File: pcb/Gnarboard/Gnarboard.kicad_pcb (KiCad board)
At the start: 2 copper layers, 184 x 136 mm, 134 parts, among them J1 N2K, J10 Screw_Terminal_01x02, J11 Screw_Terminal_01x02, J12 Screw_Terminal_01x02, J2 I2C, J3 Screw_Terminal_01x12, J4 Screw_Terminal_01x12, J5 Screw_Terminal_01x02, J6 Screw_Terminal_01x02, J7 Screw_Terminal_01x02, J8 Screw_Terminal_01x02, J9 Screw_Terminal_01x02, Q1 BC817, Q10 IRF4905, Q11 BC817, Q12 IRF4905, Q13 BC817, Q14 IRF4905, Q15 BC817, Q16 IRF4905, Q2 IRF4905, Q3 BC817, Q4 IRF4905, Q5 BC817, Q6 IRF4905, Q7 BC817, Q8 IRF4905, Q9 BC817, U1 ESP32-DEVKITC, U10 ACS725xLCTR-20AU, U11 ACS725xLCTR-20AU, U12 ACS725xLCTR-20AU, U2 MCP3208, U4 D24V5F3, U5 ACS725xLCTR-20AU, U6 ACS725xLCTR-20AU, U7 ACS725xLCTR-20AU, U8 ACS725xLCTR-20AU, U9 ACS725xLCTR-20AU

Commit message: lots of progress on new layout.
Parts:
- U10, U11, U12, U5, U6, U7, U8, U9: footprint Package_SO:SOIC-8_3.9x4.9mm_P1.27mm -> gnarboard:ACS7XX
- moved JP1 9.33 mm to (79.0, 110.5)
- moved C10 1.14 mm to (146.1, 114.8)
- moved C13 1.14 mm to (165.1, 114.8)
- moved C16 1.14 mm to (184.2, 114.8)
- moved C19 1.14 mm to (203.2, 114.8)
- moved C22 1.14 mm to (222.3, 114.8)
- moved C4 1.14 mm to (108.0, 114.8)
- moved C7 1.14 mm to (127.0, 114.8)
- moved C25 1.14 mm to (241.4, 114.8)
- moved C11 1.02 mm to (146.1, 117.2)
- moved C14 1.02 mm to (165.1, 117.2)
- moved C17 1.02 mm to (184.2, 117.2)
- moved C20 1.02 mm to (203.2, 117.2)
- moved C23 1.02 mm to (222.3, 117.2)
- moved C5 1.02 mm to (108.0, 117.2)
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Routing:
- net +24V: track 0.00 -> 325.5 mm, vias 0 -> 8
- net +3.3V: track 0.00 -> 283.8 mm, vias 0 -> 10
- net /PWM7: track 0.00 -> 191.3 mm, vias 0 -> 1
- net /ADC7: track 0.00 -> 178.2 mm, vias 0 -> 2
- net /PWM6: track 0.00 -> 173.8 mm, vias 0 -> 1
- net /ADC6: track 0.00 -> 158.1 mm, vias 0 -> 2
- net /PWM5: track 0.00 -> 155.9 mm, vias 0 -> 1
- net /ADC5: track 0.00 -> 138.3 mm, vias 0 -> 2
- net /PWM4: track 0.00 -> 136.8 mm, vias 0 -> 1
- net /ADC4: track 0.00 -> 118.5 mm, vias 0 -> 2
- net /PWM3: track 0.00 -> 117.9 mm, vias 0 -> 1
- net GNDPWR: track 0.00 -> 101.4 mm
- net /PWM2: track 0.00 -> 99.6 mm, vias 0 -> 1
- net /ADC3: track 0.00 -> 96.8 mm, vias 0 -> 2
- net +5V: track 0.00 -> 91.4 mm
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
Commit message: more progress, found a nice easy regulator too.
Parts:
- removed D1: 30V, Diode_SMD:D_SOD-123F
- removed DFR0571: ~, gnarboard:DF1768
- removed U4: D24V5F3, gnarboard:D24V5FX
- added C2: 10uF, Capacitor_SMD:C_0805_2012Metric_Pad1.18x1.45mm_HandSolder, F.Cu at (80.3, 40.4)
- added C27: 1nF, Capacitor_SMD:C_0805_2012Metric_Pad1.18x1.45mm_HandSolder, F.Cu at (76.2, 40.4)
- added D26: BZX384, Diode_SMD:D_SOD-323_HandSoldering, F.Cu at (72.1, 40.4)
- added L1: 100uH, Inductor_SMD:L_1210_3225Metric_Pad1.42x2.65mm_HandSolder, F.Cu at (84.3, 34.0)
- added U3: R-78B3.3-2.0, Converter_DCDC:Converter_DCDC_RECOM_R-78B-2.0_THT, F.Cu at (78.7, 35.6)
- C1: value 100nF -> 10uF
- J1: footprint Connector_PinSocket_2.54mm:PinSocket_1x04_P2.54mm_Vertical -> Connector_PinSocket_2.54mm:PinSocket_1x04_P2.54mm_Horizontal
- moved C1 75.5 mm to (84.3, 30.0), turned to 180 degrees
- moved J1 28.7 mm to (71.4, 114.0), turned to 0 degrees
- moved J2 20.9 mm to (64.8, 106.2)
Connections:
- C1 pad 1: +5V -> +24V
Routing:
- net +3.3V: track 283.8 -> 354.4 mm
- net SCL: track 0.00 -> 65.6 mm, vias 0 -> 1
- net SDA: track 0.00 -> 59.6 mm, vias 0 -> 1
- net CAN_TX: track 0.00 -> 56.0 mm, vias 0 -> 1
- net CAN_RX: track 0.00 -> 46.9 mm, vias 0 -> 1
- net +5V: track 91.4 -> 63.2 mm
- net Net-(U3-IN): track 0.00 -> 12.6 mm
- net Net-(D26-A): track 0.00 -> 8.08 mm
- net GNDD: track 36.6 -> 44.0 mm, vias 8 -> 10
- net +24V: track 325.5 -> 320.7 mm
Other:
- board text added: "5V"
- board text added: "GND"
- board text added: "VIN"

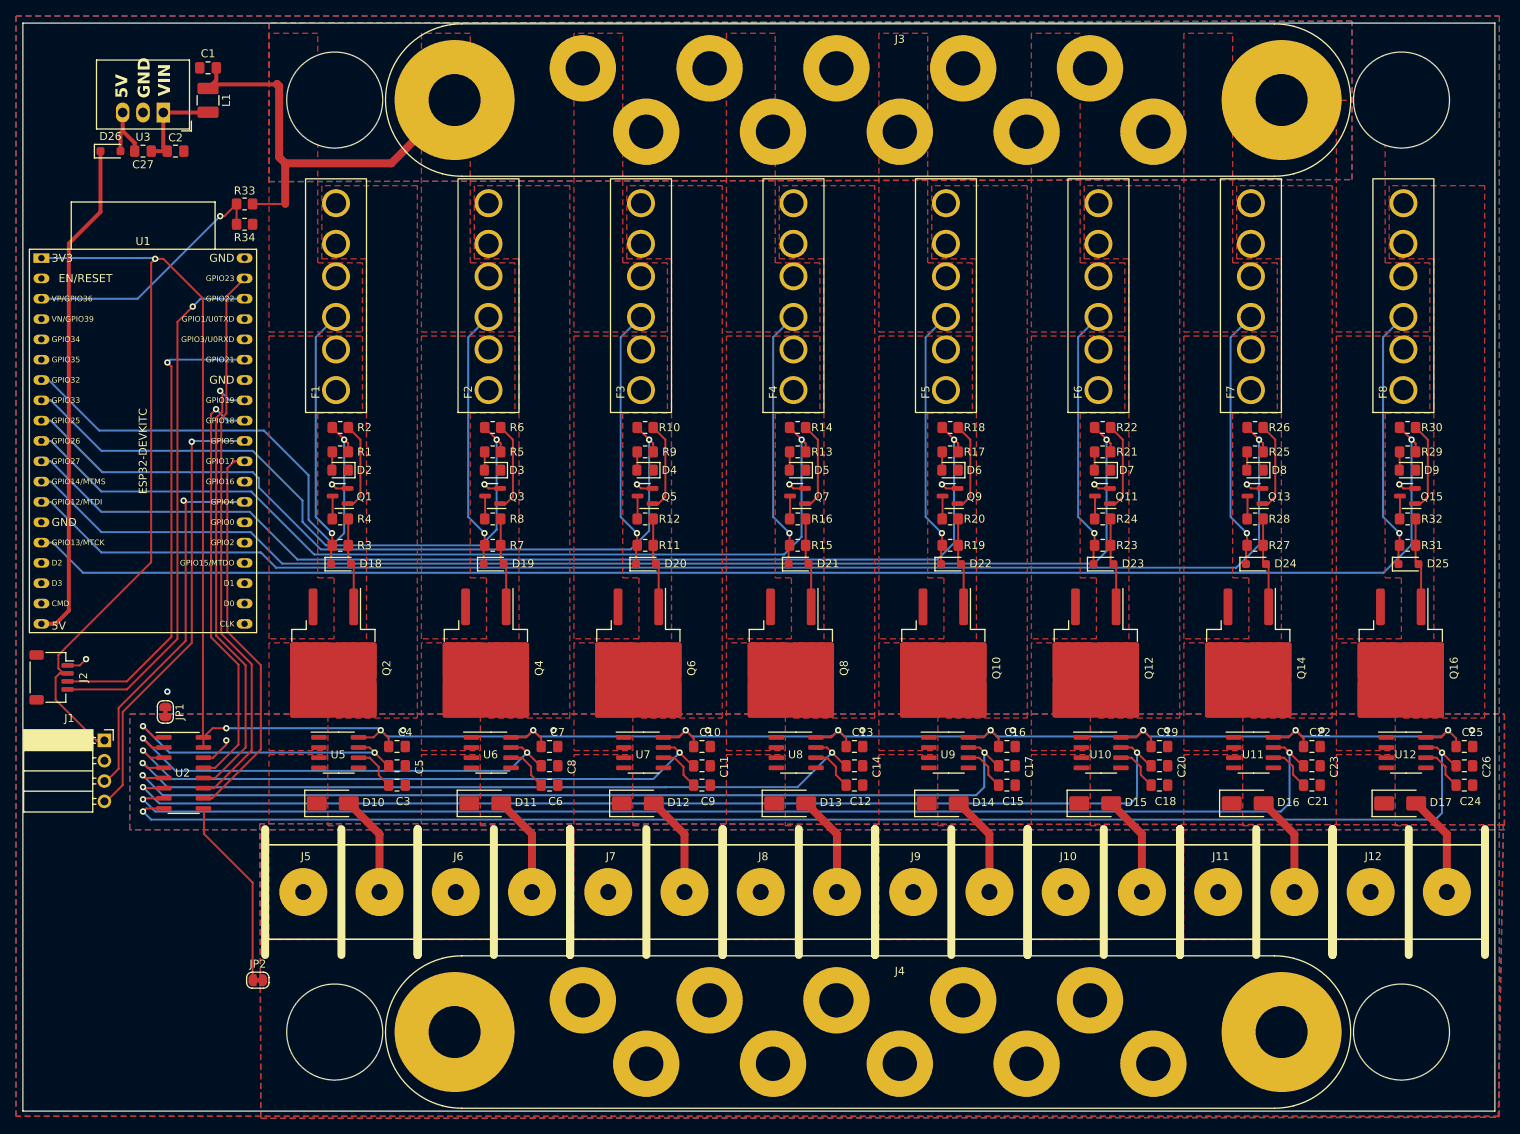
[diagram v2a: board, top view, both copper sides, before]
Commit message: added silkscreens and logos.
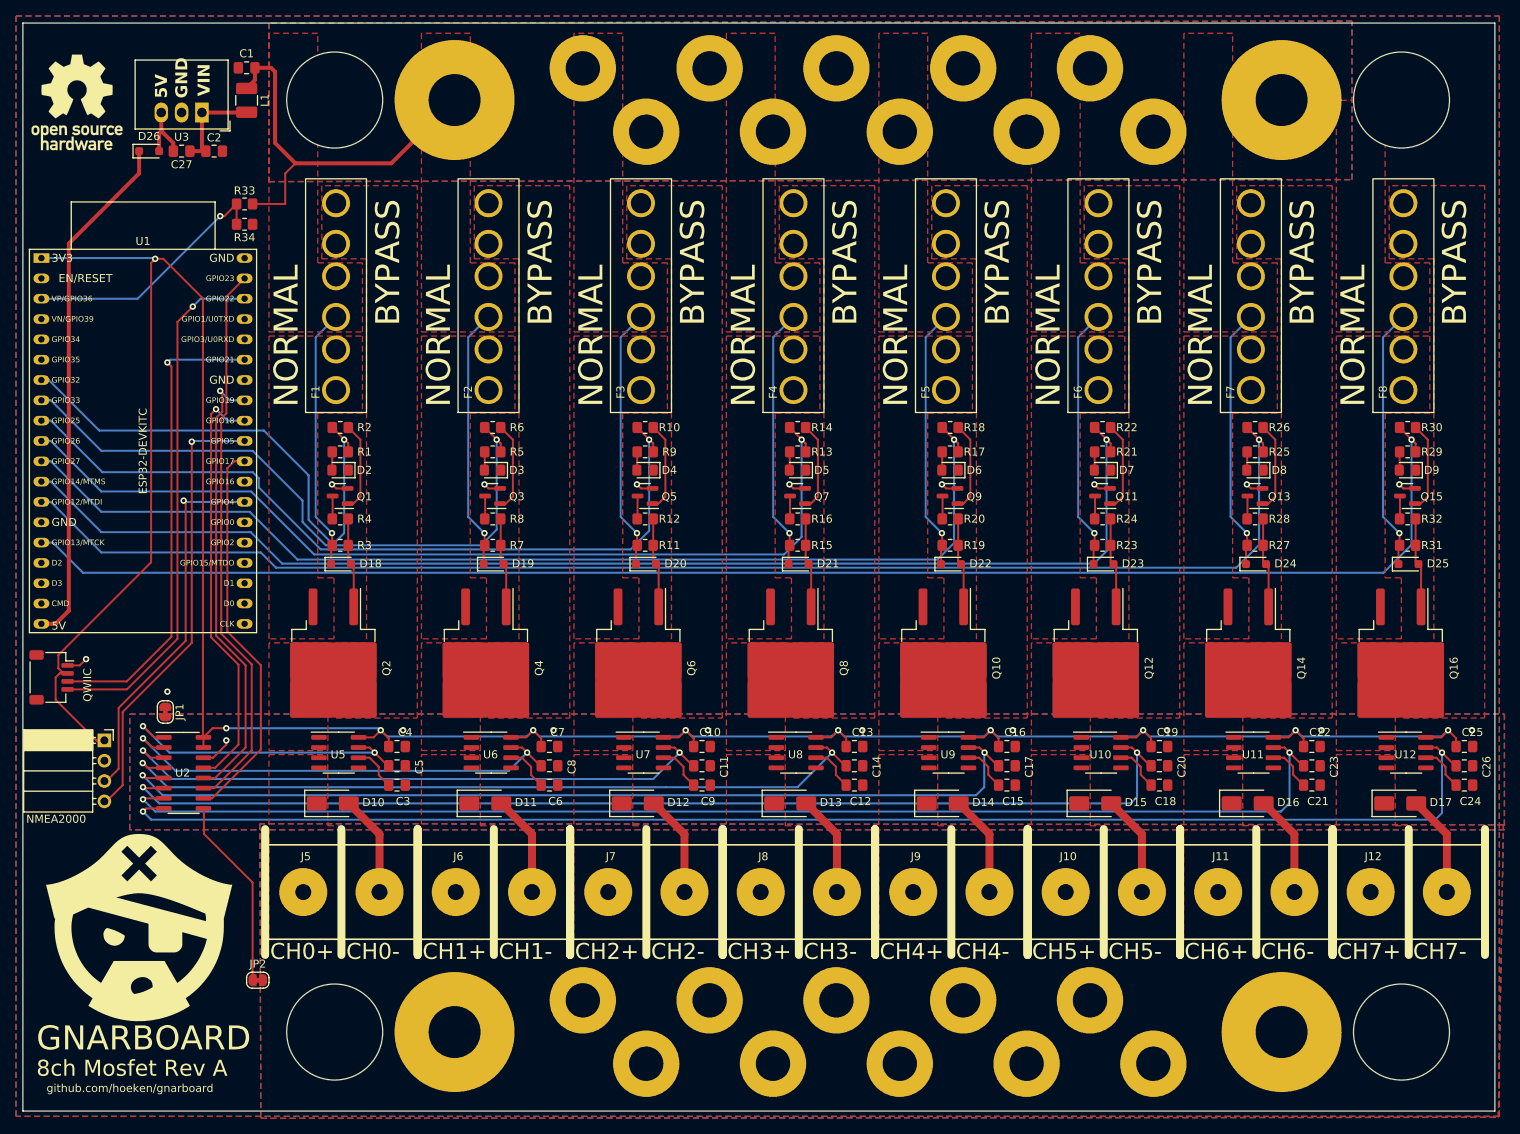
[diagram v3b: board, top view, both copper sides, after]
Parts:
- added REF**: Logo, gnarboard:Logo, F.Cu at (75.6, 138.4)
- added REF**: OSHW-Logo_11.4x12mm_SilkScreen, Symbol:OSHW-Logo_11.4x12mm_SilkScreen, F.Cu at (67.9, 34.3)
- moved C2 4.83 mm to (85.1, 40.4)
- moved D26 4.83 mm to (77.0, 40.4)
- moved U3 4.83 mm to (83.6, 35.6)
- moved C1 4.83 mm to (89.2, 30.0)
- moved C27 4.83 mm to (81.0, 40.4)
- moved L1 4.83 mm to (89.2, 34.0)
- renumbered J4 to locked
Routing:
- net +24V: track 320.7 -> 316.7 mm
- net +5V: track 63.2 -> 65.2 mm
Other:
- board text added: "8ch Mosfet Rev A"
- board text added: "BYPASS"
- board text added: "CH0+"
- board text added: "CH0-"
- board text added: "CH1+"
- board text added: "CH1-"
- board text added: "CH2+"
- board text added: "CH2-"
- board text added: "CH3+"
- board text added: "CH3-"
- board text added: "CH4+"
- board text added: "CH4-"
- board text added: "CH5+"
- board text added: "CH5-"
- board text added: "CH6+"
- board text added: "CH6-"
- board text added: "CH7+"
- board text added: "CH7-"
- board text added: "GNARBOARD"
- board text added: "NMEA2000"
- board text added: "NORMAL"
- board text added: "QWIIC"
- board text added: "github.com/hoeken/gnarboard"

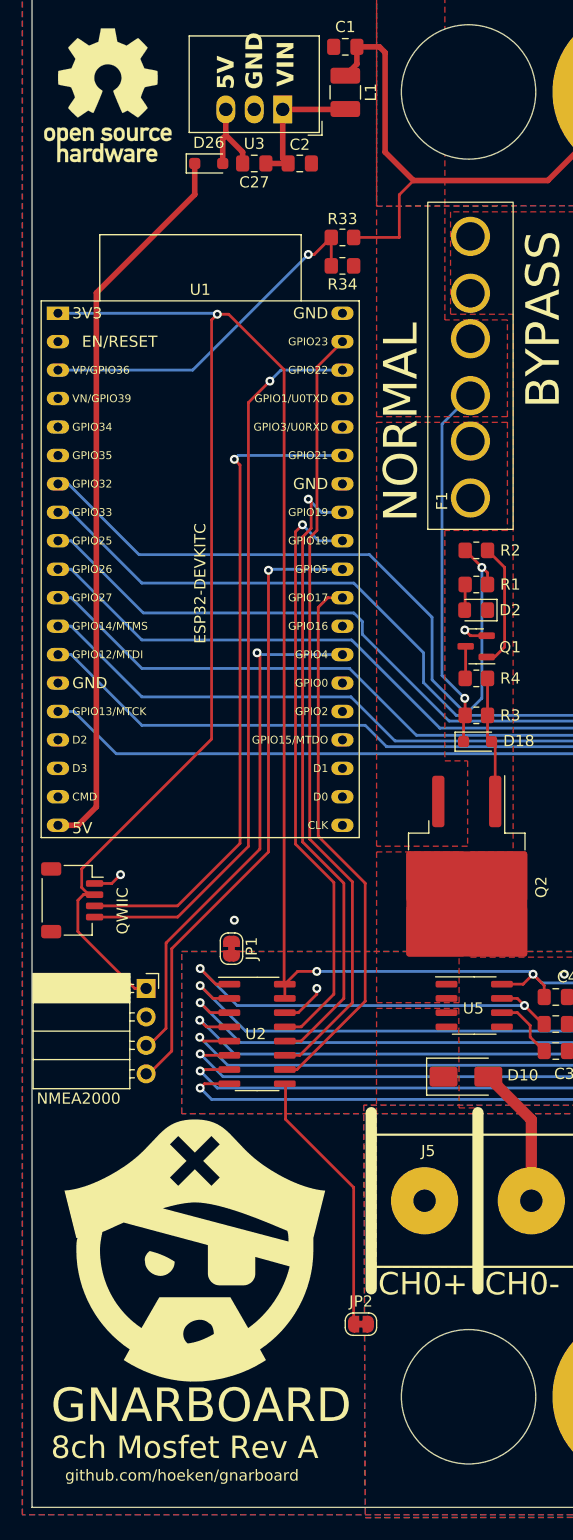
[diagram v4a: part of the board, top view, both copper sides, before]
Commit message: updated the silkscreen and n2k connector
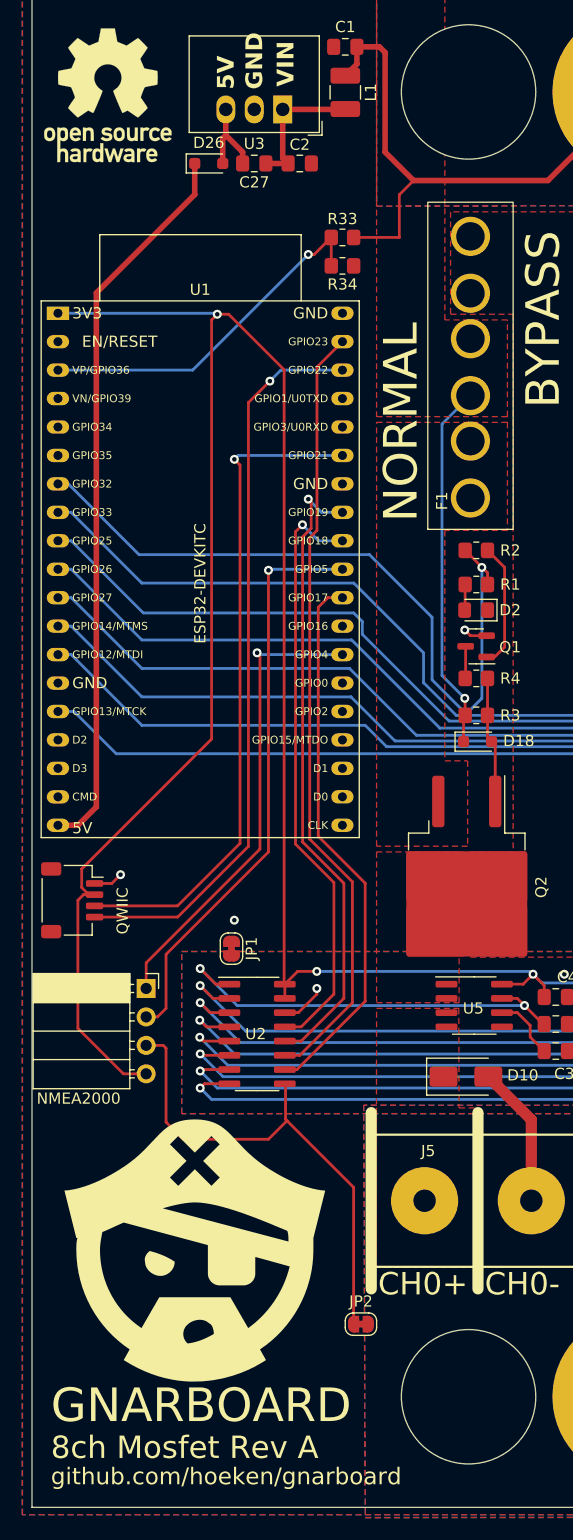
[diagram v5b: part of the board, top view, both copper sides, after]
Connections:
- J1 pad 1: +3.3V -> CAN_RX
- J1 pad 2: GNDD -> CAN_TX
- J1 pad 3: CAN_RX -> GNDD
- J1 pad 4: CAN_TX -> +3.3V
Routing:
- net GNDD: track 44.0 -> 64.6 mm
- net +3.3V: track 354.4 -> 362.3 mm
- net CAN_RX: track 46.9 -> 42.0 mm
- net CAN_TX: track 56.0 -> 51.6 mm
- net +24V: track 316.7 -> 316.0 mm

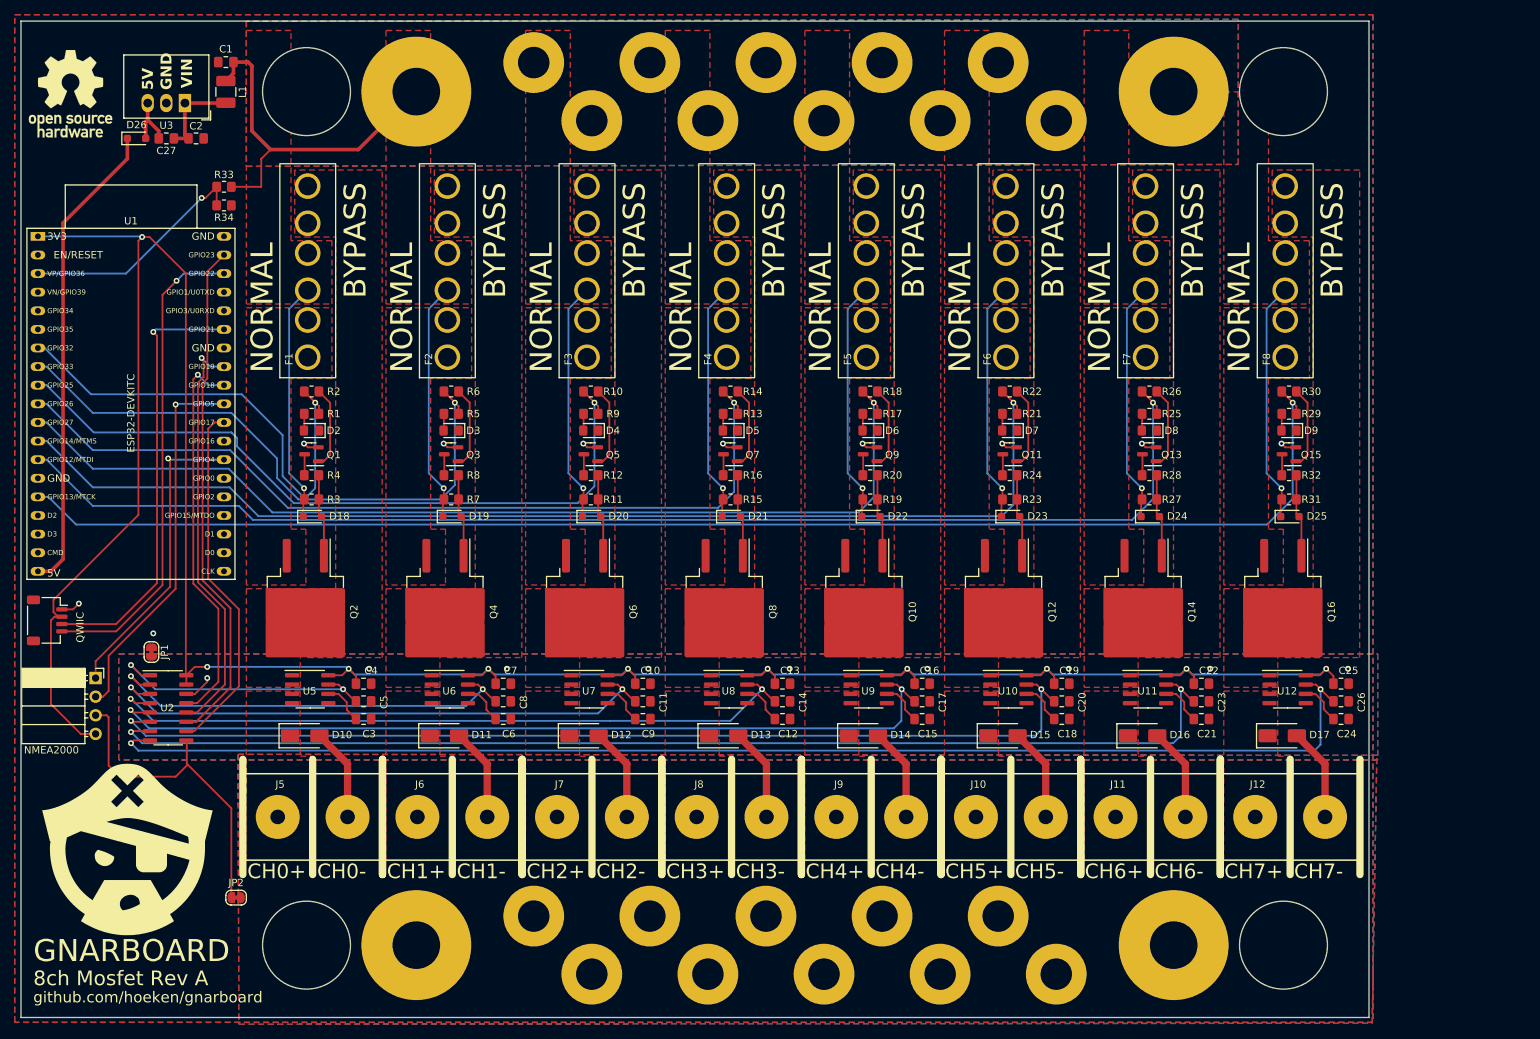
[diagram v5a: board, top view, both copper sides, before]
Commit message: changed to busbar. blueseas posts are too tall.  fml
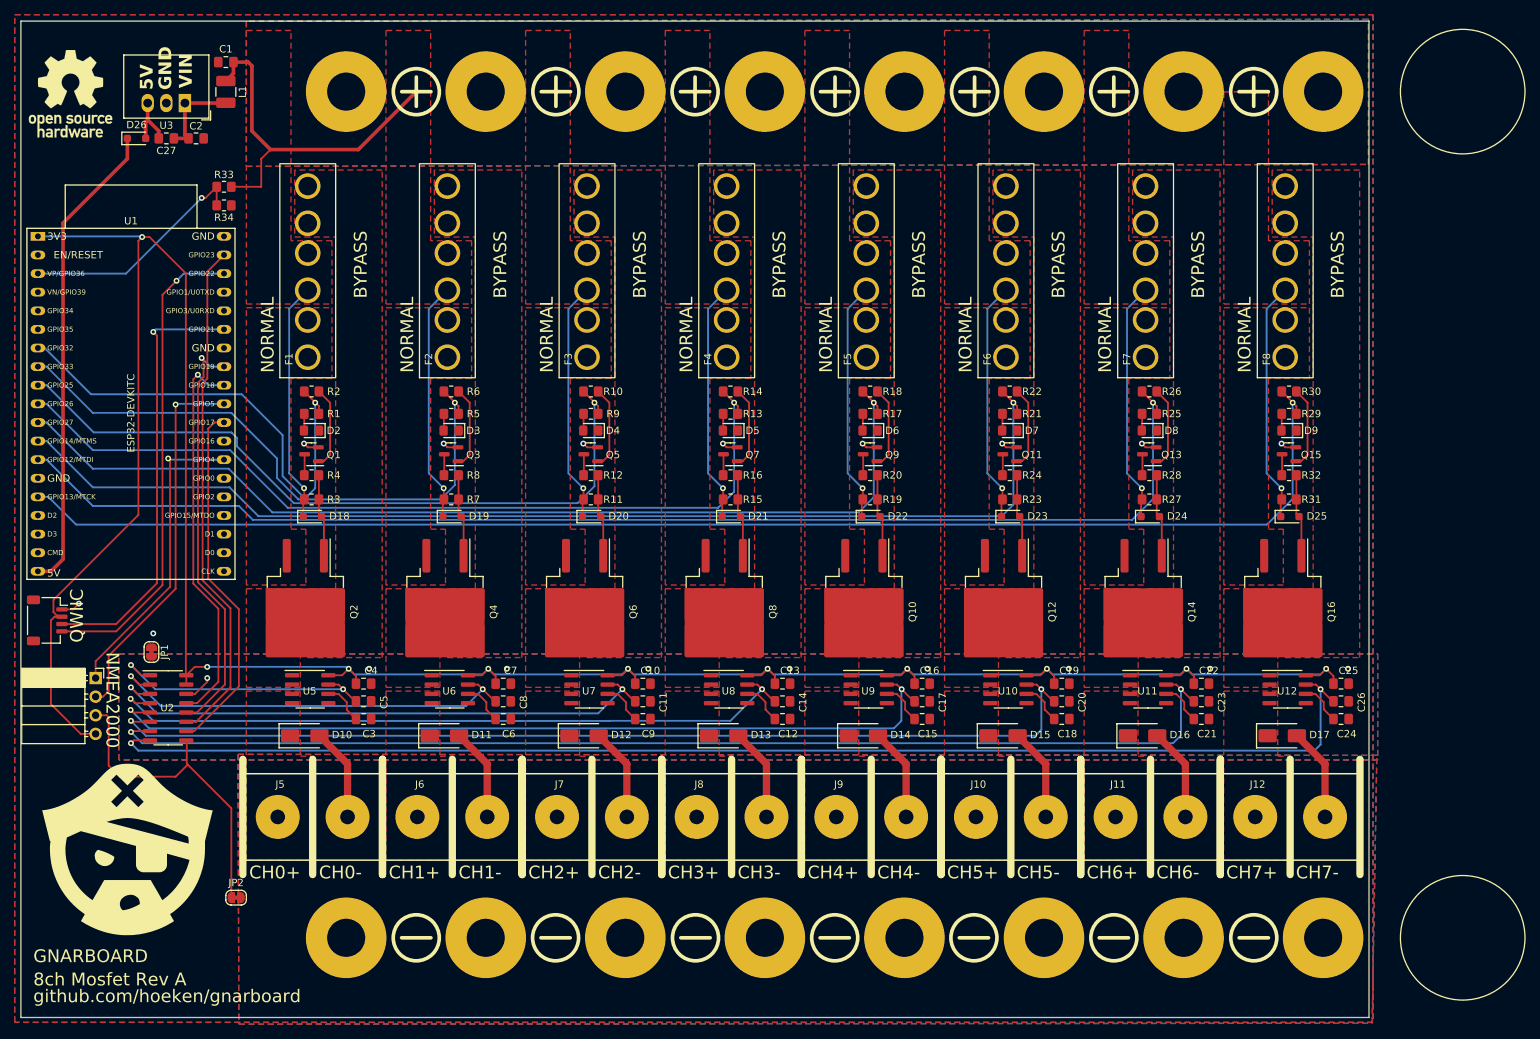
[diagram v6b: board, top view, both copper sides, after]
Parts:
- J3, locked: value Screw_Terminal_01x12 -> Screw_Terminal_01x09; footprint gnarboard:BSS 2301 -> gnarboard:Busbar 1x9 .375in
- moved locked 96.7 mm to (267.5, 149.5), turned to 180 degrees
- moved J3 96.7 mm to (267.5, 34.0), turned to 180 degrees
